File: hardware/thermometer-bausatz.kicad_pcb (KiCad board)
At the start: 2 copper layers, 100 x 50 mm, 36 parts, among them J1 TEST_1P, J2 TEST_1P, J3 ISP, U1 ATTINY24A-SSU, U2 MCP9700AT-E_TT

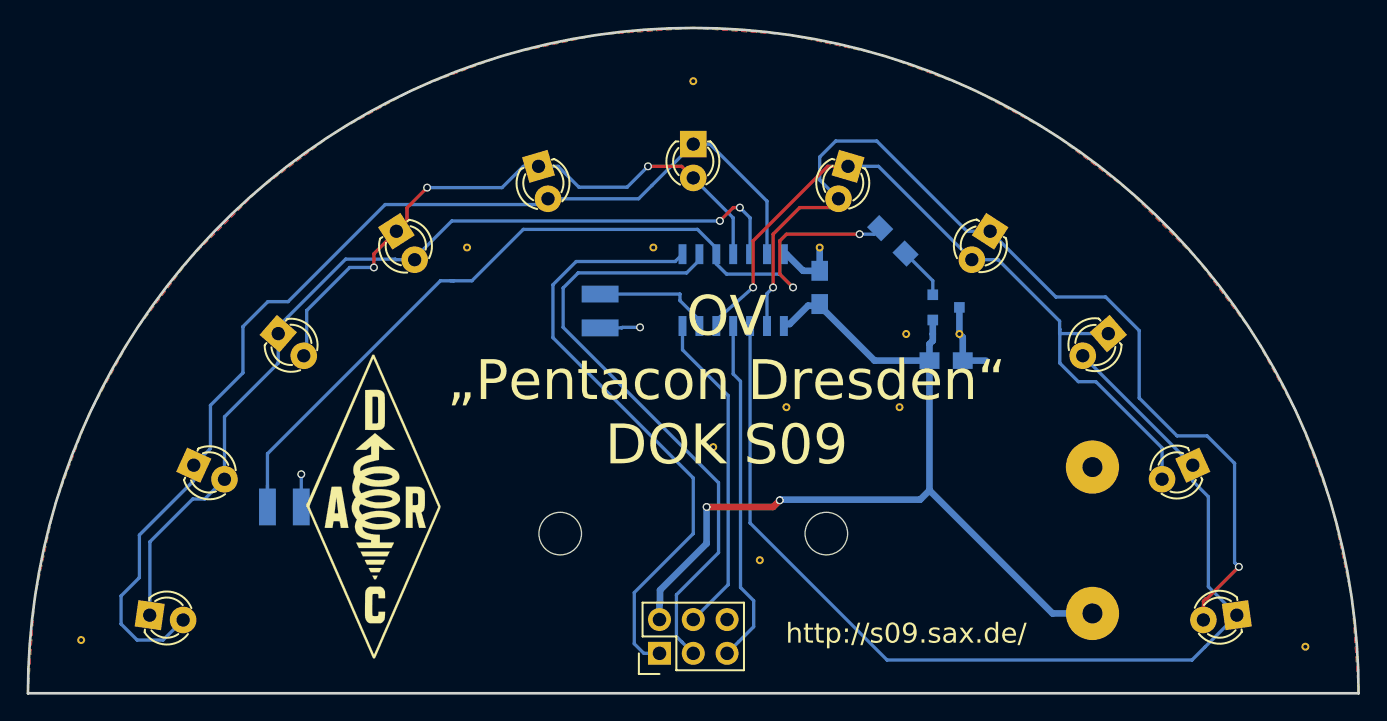
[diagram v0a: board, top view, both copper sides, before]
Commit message: Upgrade to Kicad 7
Upgrade project files.

Schematics now ends in .kicad_sch rather .sch.
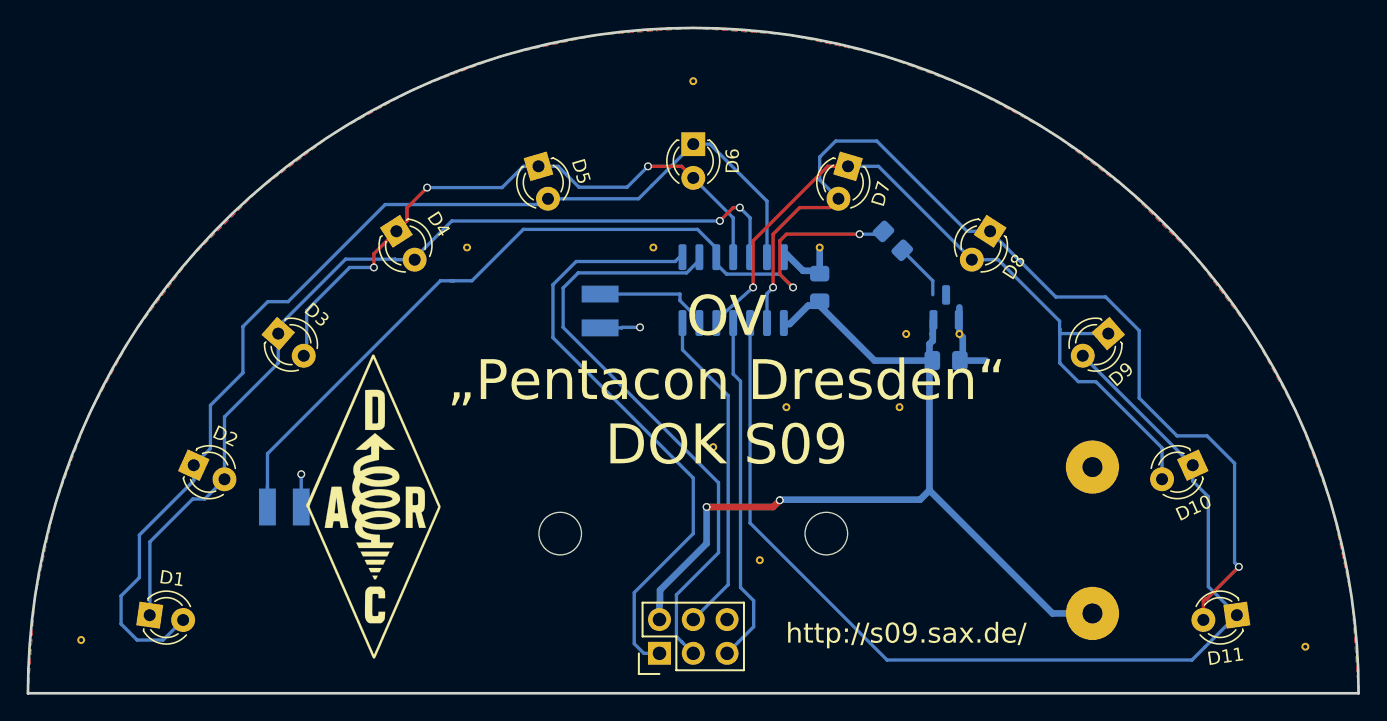
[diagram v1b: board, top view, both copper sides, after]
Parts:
- C1, C2: footprint Capacitors_SMD:C_0805_HandSoldering -> Capacitor_SMD:C_0805_2012Metric_Pad1.18x1.45mm_HandSolder
- D1, D10, D11, D2, D3, D4, D5, D6, D7, D8, D9: footprint LEDs:LED-3MM -> LED_THT:LED_D3.0mm
- R1: footprint Resistors_SMD:R_0805_HandSoldering -> Resistor_SMD:R_0805_2012Metric_Pad1.20x1.40mm_HandSolder
- U1: footprint Housings_SOIC:SOIC-14_3.9x8.7mm_Pitch1.27mm -> Package_SO:SOIC-14_3.9x8.7mm_P1.27mm
- U2: footprint TO_SOT_Packages_SMD:SOT-23 -> Package_TO_SOT_SMD:SOT-23
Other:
- net class Default removed
- net class Power removed

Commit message: Resolve DRC errors
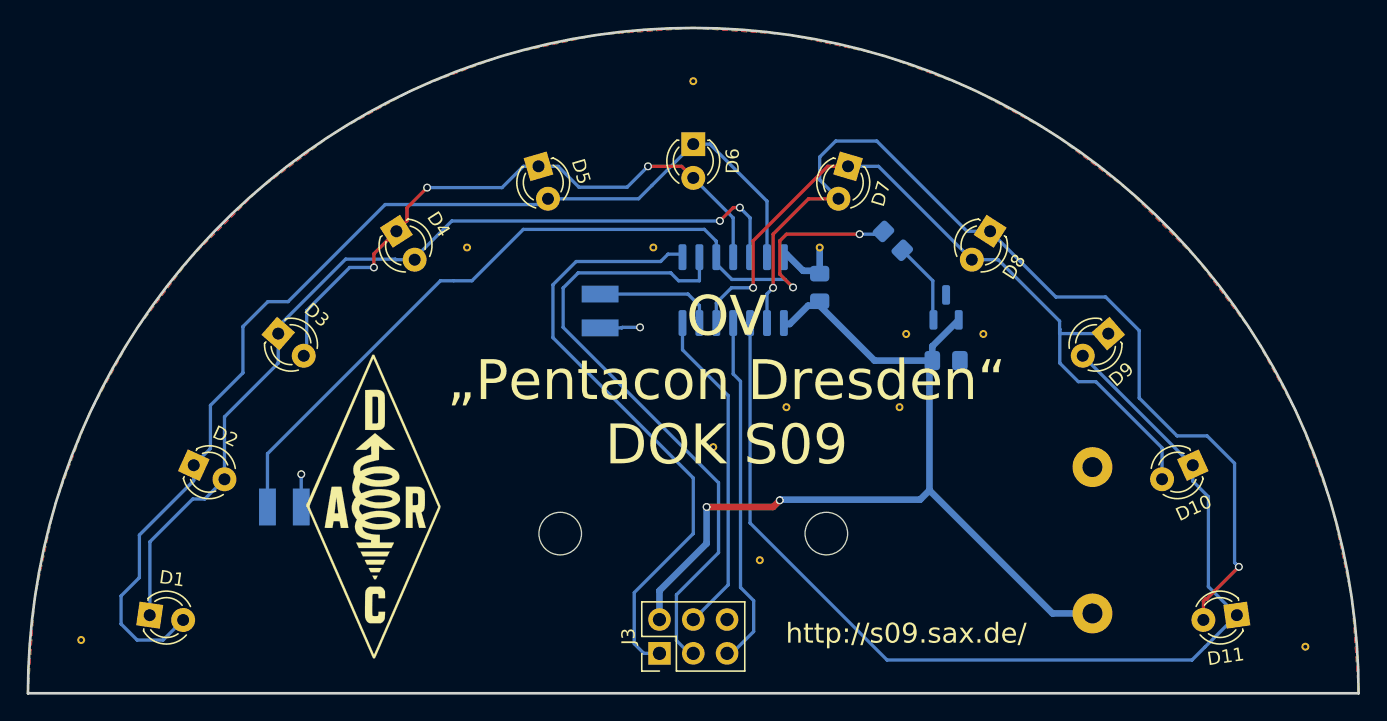
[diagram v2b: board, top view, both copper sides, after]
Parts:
- J1, J2: footprint Wire_Pads:SolderWirePad_single_1-5mmDrill -> TestPoint:TestPoint_THTPad_D3.0mm_Drill1.5mm
- J3: footprint Pin_Headers:Pin_Header_Straight_2x03 -> Connector_PinHeader_2.54mm:PinHeader_2x03_P2.54mm_Vertical
- moved N9 1.80 mm to (131.8, 133.0)
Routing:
- net GNDD: track 16.3 -> 10.4 mm
- net Net-(R1-Pad1): track 3.94 -> 6.20 mm
- net Net-(JP2-Pad1): track 66.7 -> 65.1 mm
- net Net-(J3-Pad3): track 45.7 -> 47.3 mm
- net Net-(J3-Pad4): track 25.8 -> 24.6 mm
- net Net-(J3-Pad5): track 27.3 -> 26.3 mm
- net Net-(D11-Pad2): track 75.0 -> 74.1 mm
- net Net-(D10-Pad2): track 57.7 -> 58.5 mm
- net +3V3: track 69.6 -> 70.3 mm
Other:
- rule pad_to_mask_clearance: 0.2 -> 0.05

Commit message: Add QR code for URL
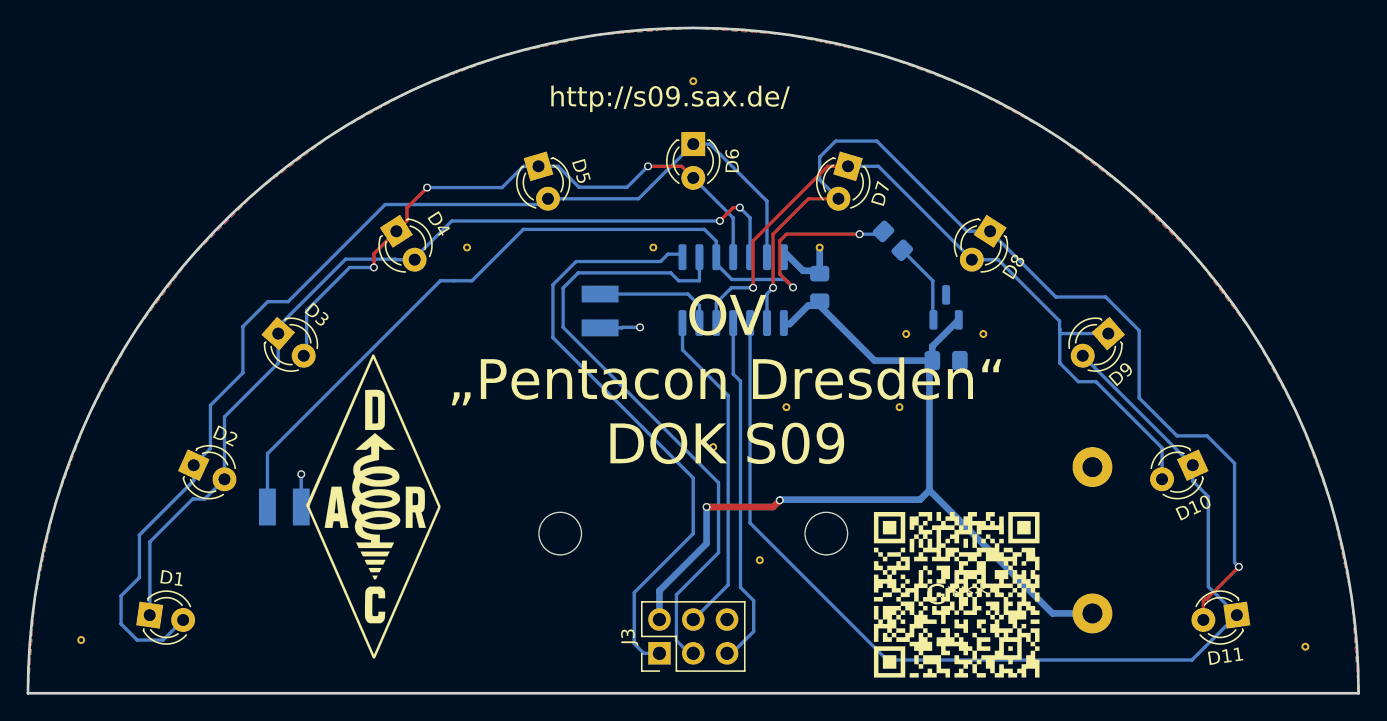
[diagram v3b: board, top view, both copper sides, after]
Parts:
- added G***: LOGO, Thermometer-Bausatz:bastelecke-url, F.Cu at (129.8, 152.6)

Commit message: Modernize everything
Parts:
- removed the G*** at (129.8, 152.6)
- added B2: ~, Thermometer-Bausatz:bastelecke-url, F.Cu at (130.5, 152.2)
- moved REF** 0.83 mm to (118.8, 118.0)

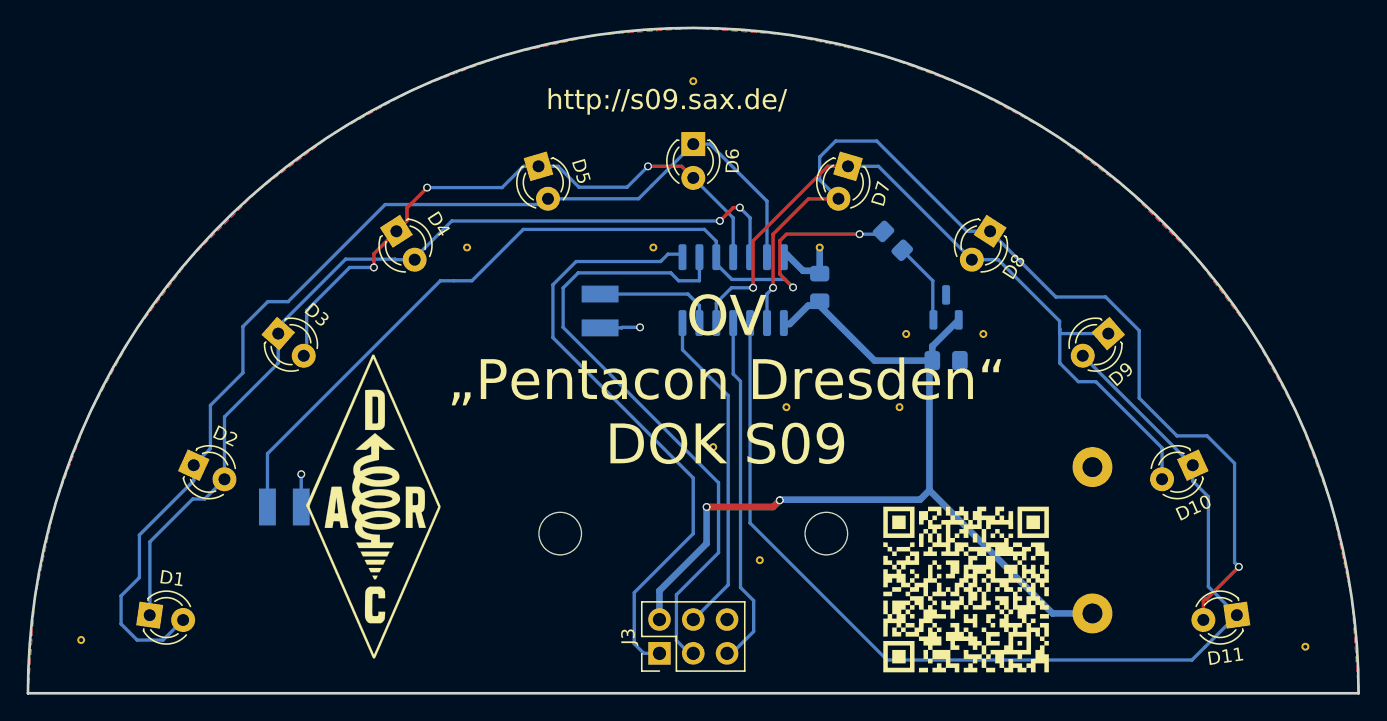
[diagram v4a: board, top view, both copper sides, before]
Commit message: Replace ATtiny24 by AVR16EB14
While both controllers share the same footprint, the AVR16EB14
is quite a bit different. To begin, the footprints have VDD and
GND swapped. The AVRxEB uses UPDI for programming, so basically
only a single wire is needed. The GPIOs are scattered across
more ports. Finally, the entire clock system and ADC is
different.
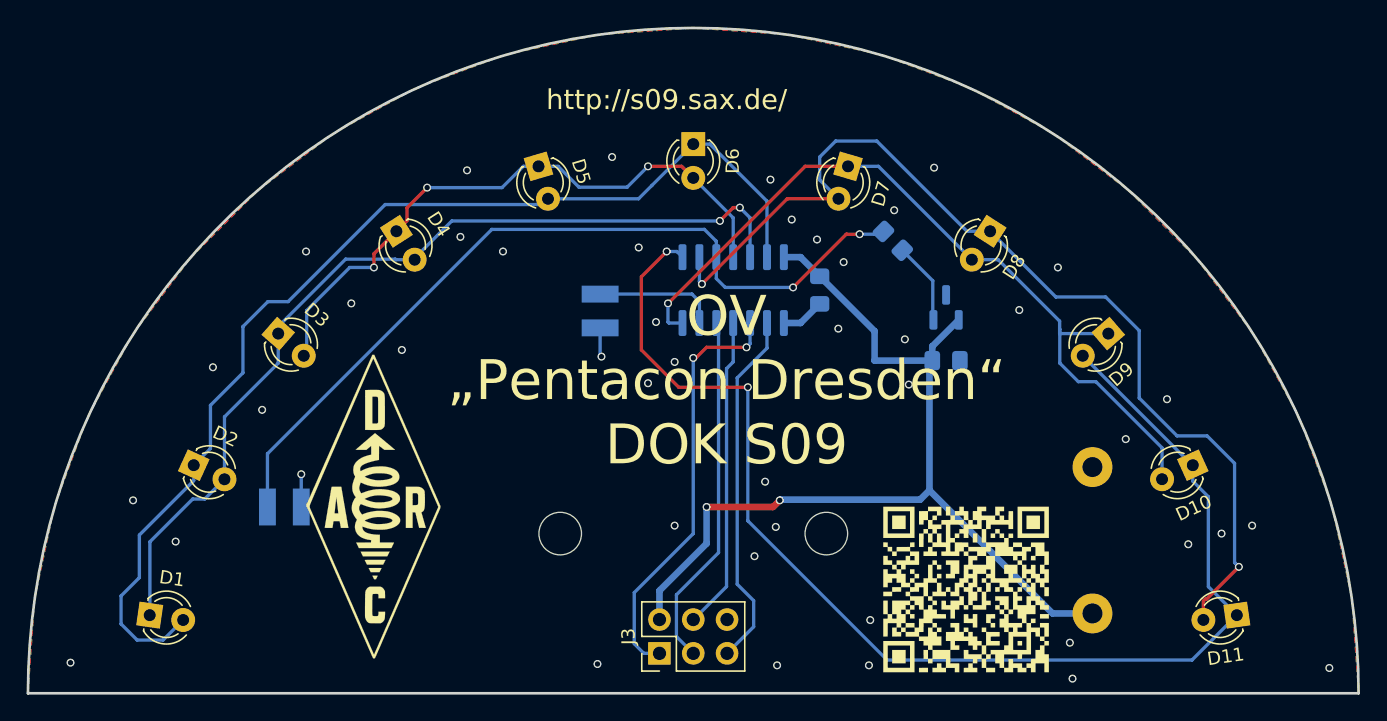
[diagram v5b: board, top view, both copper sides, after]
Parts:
- removed G***: LOGO, Thermometer-Bausatz:DARC-Raute
- removed N1, N10, N11, N12, N2, N3, N4, N5, N6, N7, N8, N9: via, Thermometer-Bausatz:via-0.3-0.6
- removed REF**: RoHS_Silk, Thermometer-Bausatz:RoHS_Silk
- added B3: DARC-Logo, Thermometer-Bausatz:DARC-Raute, F.Cu at (86.0, 146.0)
- added B4: RoHS-Logo, Thermometer-Bausatz:RoHS_Silk, B.Cu at (118.0, 118.0)
- J3: value ISP -> UPDI
- moved C1 0.20 mm to (119.5, 129.7), turned to -90 degrees
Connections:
- U1 pad 1: +3V3 -> GNDD
- U1 pad 14: GNDD -> +3V3
- U1 pad 2: Net-(D11-A) -> Net-(J3-Pin_5)
- U1 pad 3: Net-(D10-K) -> Net-(J3-Pin_1)
- U1 pad 4: Net-(J3-Pin_5) -> Net-(J3-Pin_4)
- U1 pad 5: Net-(D10-A) -> Net-(J3-Pin_3)
- U1 pad 7: Net-(J3-Pin_4) -> Net-(D10-A)
- U1 pad 8: Net-(J3-Pin_1) -> Net-(D10-K)
- U1 pad 9: Net-(J3-Pin_3) -> Net-(D11-A)
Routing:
- net Net-(J3-Pin_3): track 47.3 -> 26.7 mm
- net Net-(J3-Pin_1): track 46.1 -> 31.8 mm, vias 0 -> 2
- net Net-(D10-K): track 81.4 -> 95.5 mm, vias 0 -> 2
- net Net-(U1-PD4): track 65.1 -> 62.3 mm
- net Net-(D11-A): track 74.1 -> 76.7 mm
- net GNDD: track 10.4 -> 7.95 mm, vias 2 -> 45
- net Net-(D10-A): track 58.5 -> 60.9 mm
- net +3V3: track 70.3 -> 72.4 mm
- net Net-(J3-Pin_4): track 24.6 -> 23.5 mm
- net Net-(J3-Pin_5): track 26.3 -> 27.1 mm

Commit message: Remove external temperature sensor
The external sensor was initially designed as an option to allow for a
more accurate temperature sensor. To save part costs, it has never
actually been implemented.

With the AVRxEB, the internal temperature sensor comes pre-calibrated
(through fuse values), so it is safe to get rid of that idea
entirely.
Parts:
- removed C2: 100 nF, Capacitor_SMD:C_0805_2012Metric_Pad1.18x1.45mm_HandSolder
- removed R1: 4.7 kΩ, Resistor_SMD:R_0805_2012Metric_Pad1.20x1.40mm_HandSolder
- removed U2: MCP9700AT-E_TT, Package_TO_SOT_SMD:SOT-23
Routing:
- net Net-(U1-PD4): track 62.3 -> 46.3 mm, vias 2 -> 0
- net Net-(U2-Vout): track 6.20 -> 0.00 mm
- net +3V3: track 72.4 -> 68.8 mm
